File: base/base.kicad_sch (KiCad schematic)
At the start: 30 parts, among them J1 USB_B_Micro, J2 Conn_01x06, SW1 SW_Push_Open, SW2 SW_Push_Open, U1 ESP32-WROOM-32, U2 MCP73831-3-OT, U3 BMP280, U4 TPS63001

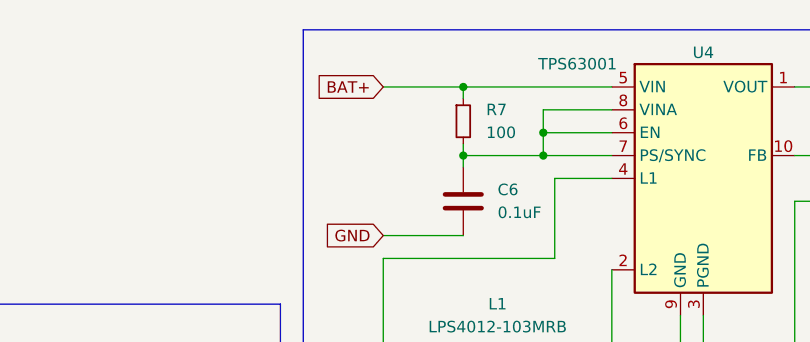
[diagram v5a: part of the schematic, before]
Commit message: fix battery charging
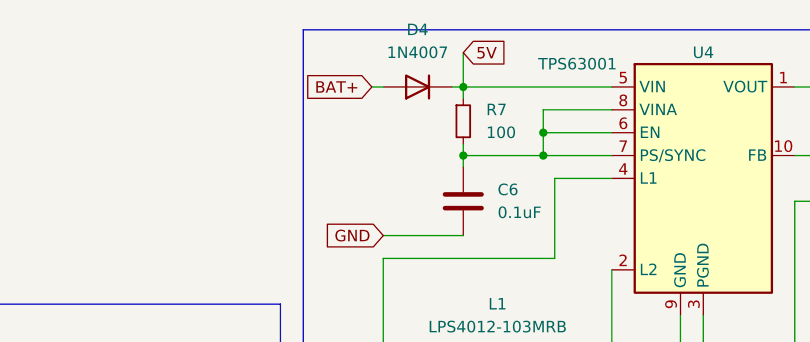
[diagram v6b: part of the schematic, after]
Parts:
- added D4: 1N4007, Diode_THT:D_DO-41_SOD81_P10.16mm_Horizontal, symbol Diode:1N4007
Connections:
- net 5V: now also R7.1, U4.5 (VIN), D4.1 (K)
- net BAT+: now also D4.2 (A); no longer R7.1, U4.5 (VIN)
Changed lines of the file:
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@@
   (junction (at 109.22 135.89) (diameter 0) (color 0 0 0 0)
   )
+  (junction (at 222.25 25.4) (diameter 0) (color 0 0 0 0)
+  )
+  (junction (at 105.41 135.89) (diameter 0) (color 0 0 0 0)
+  )
   (junction (at 213.36 20.32) (diameter 0) (color 0 0 0 0)
   )
-  (junction (at 222.25 25.4) (diameter 0) (color 0 0 0 0)
-  )
-  (junction (at 105.41 135.89) (diameter 0) (color 0 0 0 0)
-  )
   (junction (at 109.22 149.86) (diameter 0) (color 0 0 0 0)
   )
@@
     (stroke (width 0) (type default) (color 0 0 0 0))
   )
-  (wire (pts (xy 204.47 20.32) (xy 213.36 20.32))
-    (stroke (width 0) (type default) (color 0 0 0 0))
-  )
   (wire (pts (xy 213.36 27.94) (xy 213.36 29.21))
     (stroke (width 0) (type default) (color 0 0 0 0))
@@
     (stroke (width 0) (type default) (color 0 0 0 0))
   )
+  (wire (pts (xy 212.09 20.32) (xy 213.36 20.32))
+    (stroke (width 0) (type default) (color 0 0 0 0))
+  )
   (wire (pts (xy 120.65 135.89) (xy 123.19 135.89))
     (stroke (width 0) (type default) (color 0 0 0 0))
@@
     (stroke (width 0) (type default) (color 0 0 0 0))
   )
+  (wire (pts (xy 213.36 16.51) (xy 213.36 20.32))
+    (stroke (width 0) (type default) (color 0 0 0 0))
+  )
   (wire (pts (xy 265.43 20.32) (xy 265.43 21.59))
     (stroke (width 0) (type default) (color 0 0 0 0))
@@
   )
   (wire (pts (xy 156.21 49.53) (xy 158.75 49.53))
+    (stroke (width 0) (type default) (color 0 0 0 0))
+  )
+  (wire (pts (xy 203.2 20.32) (xy 204.47 20.32))
     (stroke (width 0) (type default) (color 0 0 0 0))
   )
@@
     )
   )
-  (global_label "BAT+" (shape input) (at 204.47 20.32 180) (fields_autoplaced)
-    (effects (font (size 1.27 1.27)) (justify right))
-    (property "Intersheet References" "${INTERSHEET_REFS}" (id 0) (at 197.1583 20.2406 0)
+  (global_label "BAT+" (shape input) (at 203.2 20.32 180) (fields_autoplaced)
+    (effects (font (size 1.27 1.27)) (justify right))
+    (property "Intersheet References" "${INTERSHEET_REFS}" (id 0) (at 195.8883 20.2406 0)
       (effects (font (size 1.27 1.27)) (justify right) hide)
     )
@@
     (property "Intersheet References" "${INTERSHEET_REFS}" (id 0) (at 103.3598 32.9406 0)
       (effects (font (size 1.27 1.27)) (justify right) hide)
+    )
+  )
+  (global_label "5V" (shape input) (at 213.36 16.51 0) (fields_autoplaced)
+    (effects (font (size 1.27 1.27)) (justify left))
+    (property "Intersheet References" "${INTERSHEET_REFS}" (id 0) (at 218.0712 16.4306 0)
+      (effects (font (size 1.27 1.27)) (justify left) hide)
     )
   )
@@
     (pin "2")
   )
+  (symbol (lib_id "Diode:1N4007") (at 208.28 20.32 180) (unit 1)
+    (in_bom yes) (on_board yes) (fields_autoplaced)
+    (property "Reference" "D4" (id 0) (at 208.28 13.97 0))
+    (property "Value" "1N4007" (id 1) (at 208.28 16.51 0))
+    (property "Footprint" "Diode_THT:D_DO-41_SOD81_P10.16mm_Horizontal" (id 2) (at 208.28 15.875 0)
+      (effects (font (size 1.27 1.27)) hide)
+    )
+    (property "Datasheet" "http://www.vishay.com/docs/88503/1n4001.pdf" (id 3) (at 208.28 20.32 0)
+      (effects (font (size 1.27 1.27)) hide)
+    )
+    (pin "1")
+    (pin "2")
+  )
   (symbol (lib_id "Switch:SW_Push_Open") (at 92.71 58.42 0) (unit 1)
     (in_bom yes) (on_board yes) (fields_autoplaced)
@@
       (reference "D3") (unit 1) (value "LED") (footprint "LED_SMD:LED_0603_1608Metric")
     )
+    (path "/9cf04930-92e2-4361-96fe-0e85f3c4b63b"
+      (reference "D4") (unit 1) (value "1N4007") (footprint "Diode_THT:D_DO-41_SOD81_P10.16mm_Horizontal")
+    )
     (path "/526ad245-495a-410f-92ad-a49c640f698d"

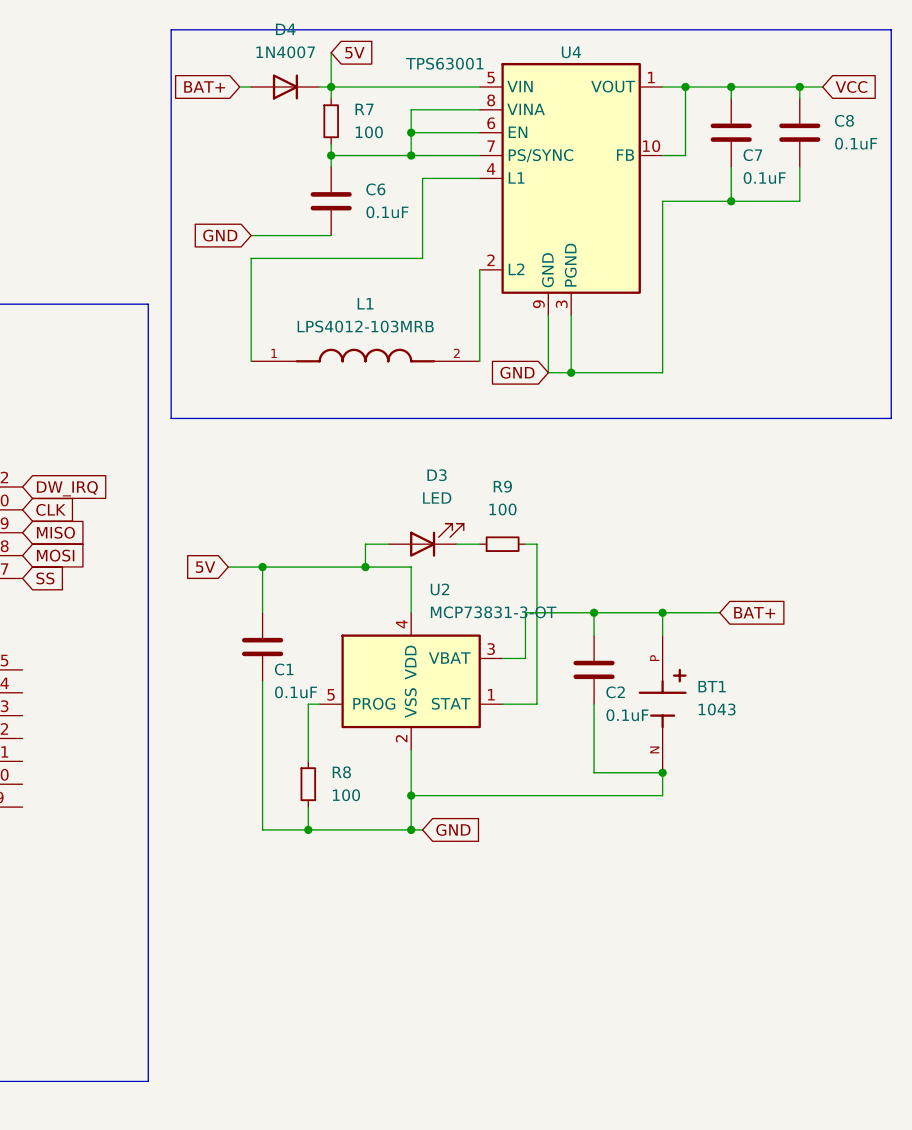
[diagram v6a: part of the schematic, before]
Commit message: fix battery charging
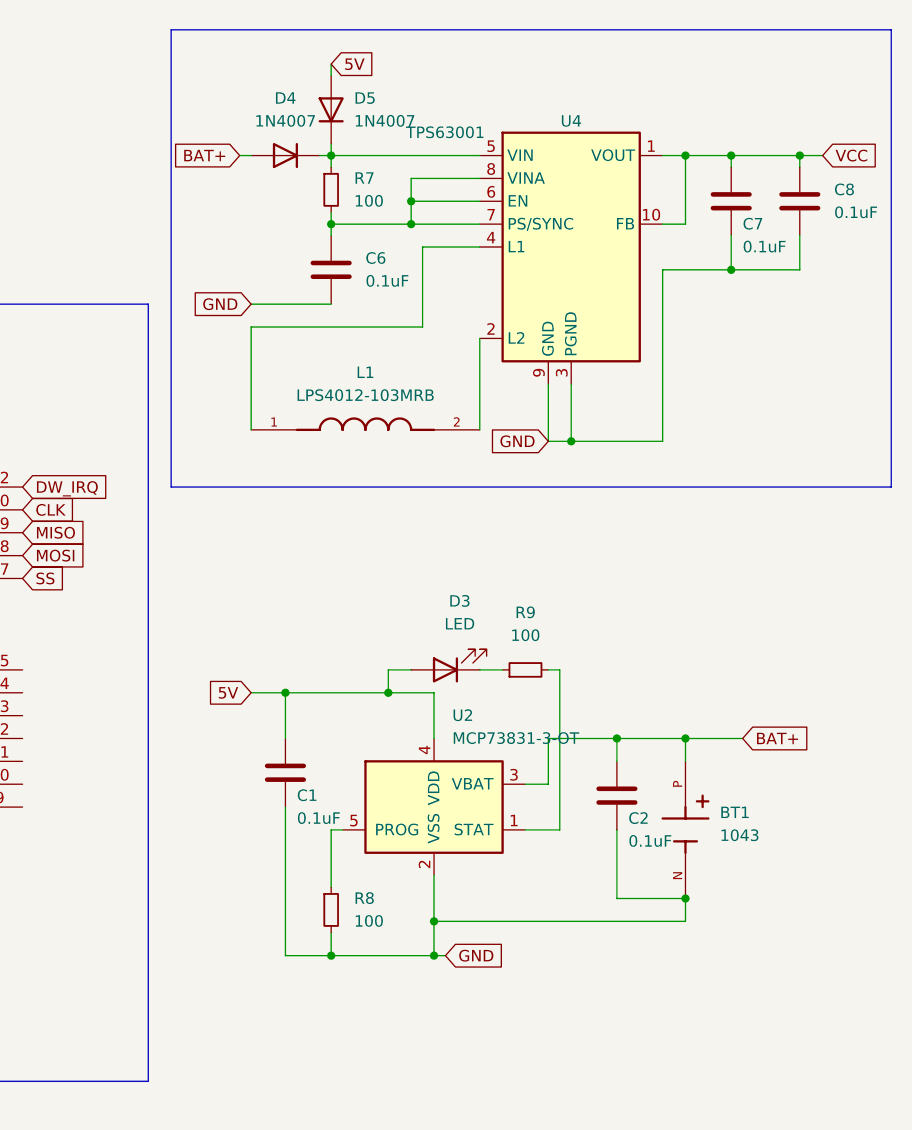
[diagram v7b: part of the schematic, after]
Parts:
- added D5: 1N4007, Fuse:Fuse_0603_1608Metric_Pad1.05x0.95mm_HandSolder, symbol Diode:1N4007
- D4: footprint Diode_THT:D_DO-41_SOD81_P10.16mm_Horizontal -> Fuse:Fuse_0603_1608Metric_Pad1.05x0.95mm_HandSolder
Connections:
- net 5V: now also D5.2 (A); no longer D4.1 (K), R7.1, U4.5 (VIN)
- new net: D4.1 (K), D5.1 (K), R7.1, U4.5 (VIN)
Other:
- moved on the sheet: BT1, C1, C2, C6, C7, C8, D3, D4, L1, R7, R8, R9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

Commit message: change diode footprint
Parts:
- D4, D5: footprint Fuse:Fuse_0603_1608Metric_Pad1.05x0.95mm_HandSolder -> Diode_SMD:Nexperia_CFP3_SOD-123W
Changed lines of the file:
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@@
       (effects (font (size 1.27 1.27)))
     )
-    (property "Footprint" "Fuse:Fuse_0603_1608Metric_Pad1.05x0.95mm_HandSolder" (at 208.28 23.495 0)
+    (property "Footprint" "Diode_SMD:Nexperia_CFP3_SOD-123W" (at 208.28 23.495 0)
       (effects (font (size 1.27 1.27)) hide)
     )
@@
       (effects (font (size 1.27 1.27)) (justify right))
     )
-    (property "Footprint" "Fuse:Fuse_0603_1608Metric_Pad1.05x0.95mm_HandSolder" (at 217.805 22.86 0)
+    (property "Footprint" "Diode_SMD:Nexperia_CFP3_SOD-123W" (at 217.805 22.86 0)
       (effects (font (size 1.27 1.27)) hide)
     )
